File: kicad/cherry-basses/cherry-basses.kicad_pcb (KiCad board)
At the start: 2 copper layers, 175 x 53 mm, 42 parts, among them SW1.1 SPST, SW1.2 SPST, SW1.3 SPST, SW1.4 SPST, SW1.5 SPST, SW1.6 SPST, SW1.7 SPST, SW1.8 SPST, SW2.0 SPST, SW2.1 SPST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

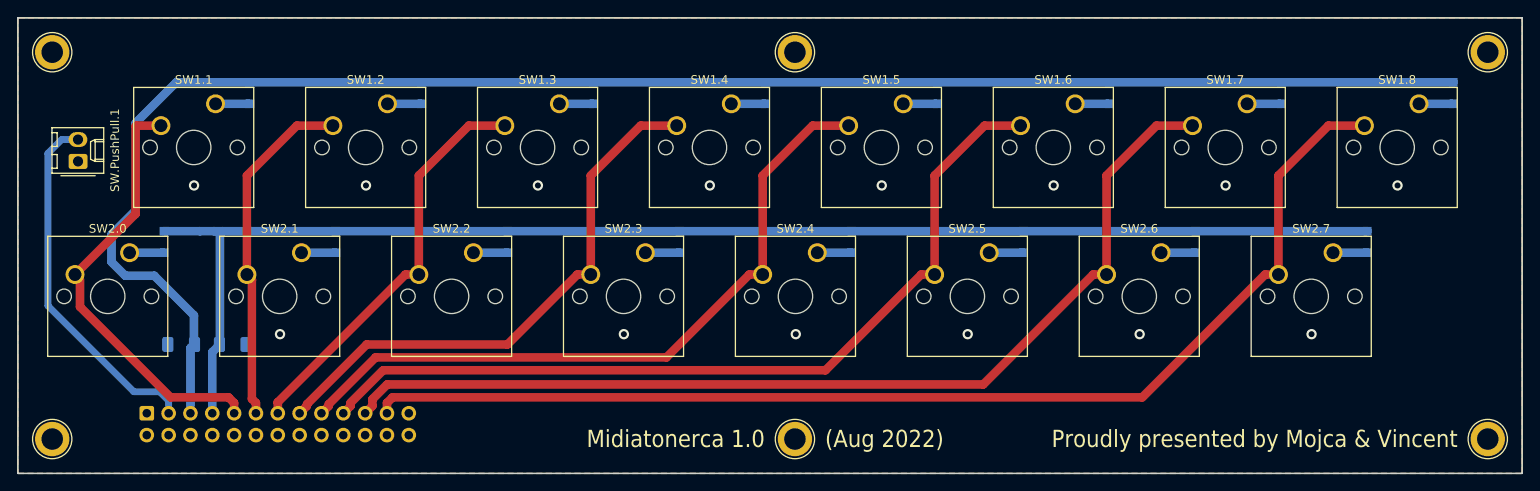
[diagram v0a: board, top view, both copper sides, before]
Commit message: cherry basses: update color, fix diode orientation, remove border from silk screen
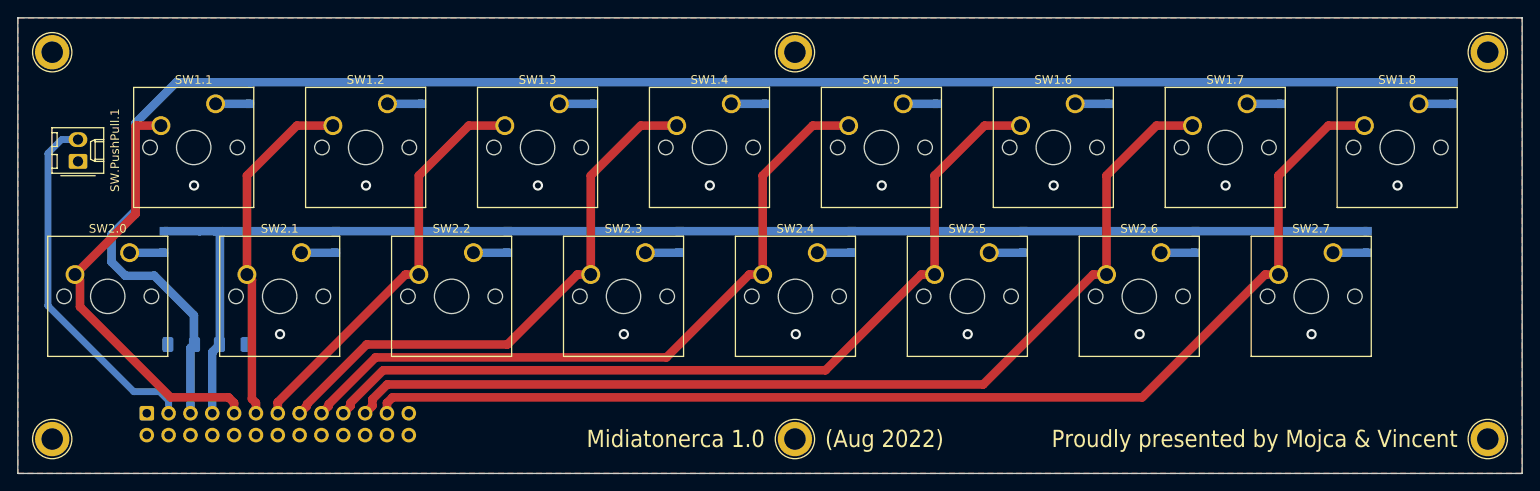
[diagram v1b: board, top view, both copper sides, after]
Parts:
- D1.1, D1.2, D1.3, D1.4, D1.5, D1.6, D1.7, D1.8, D2.0, D2.1, D2.2, D2.3, D2.4, D2.5, D2.6, D2.7: value DIODE -> 1N5819WS
- turned D1.1 to -90 degrees
- turned D1.2 to -90 degrees
- turned D1.3 to -90 degrees
- turned D1.4 to -90 degrees
- turned D1.5 to -90 degrees
- turned D1.6 to -90 degrees
- turned D1.7 to -90 degrees
- turned D1.8 to -90 degrees
- turned D2.0 to -90 degrees
- turned D2.1 to -90 degrees
- turned D2.2 to -90 degrees
- turned D2.3 to -90 degrees
- turned D2.4 to -90 degrees
- turned D2.5 to -90 degrees
- turned D2.6 to -90 degrees
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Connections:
- D1.1 pad 1: Net-(D1.1-Pad1) -> arduino_D3
- D1.1 pad 2: arduino_D3 -> Net-(D1.1-Pad2)
- D1.2 pad 1: Net-(D1.2-Pad1) -> arduino_D3
- D1.2 pad 2: arduino_D3 -> Net-(D1.2-Pad2)
- D1.3 pad 1: Net-(D1.3-Pad1) -> arduino_D3
- D1.3 pad 2: arduino_D3 -> Net-(D1.3-Pad2)
- D1.4 pad 1: Net-(D1.4-Pad1) -> arduino_D3
- D1.4 pad 2: arduino_D3 -> Net-(D1.4-Pad2)
- D1.5 pad 1: Net-(D1.5-Pad1) -> arduino_D3
- D1.5 pad 2: arduino_D3 -> Net-(D1.5-Pad2)
- D1.6 pad 1: Net-(D1.6-Pad1) -> arduino_D3
- D1.6 pad 2: arduino_D3 -> Net-(D1.6-Pad2)
- D1.7 pad 1: Net-(D1.7-Pad1) -> arduino_D3
- D1.7 pad 2: arduino_D3 -> Net-(D1.7-Pad2)
- D1.8 pad 1: Net-(D1.8-Pad1) -> arduino_D3
- D1.8 pad 2: arduino_D3 -> Net-(D1.8-Pad2)
- D2.0 pad 1: Net-(D2.0-Pad1) -> arduino_D4
- D2.0 pad 2: arduino_D4 -> Net-(D2.0-Pad2)
- D2.1 pad 1: Net-(D2.1-Pad1) -> arduino_D4
- D2.1 pad 2: arduino_D4 -> Net-(D2.1-Pad2)
- D2.2 pad 1: Net-(D2.2-Pad1) -> arduino_D4
- D2.2 pad 2: arduino_D4 -> Net-(D2.2-Pad2)
- D2.3 pad 1: Net-(D2.3-Pad1) -> arduino_D4
- D2.3 pad 2: arduino_D4 -> Net-(D2.3-Pad2)
- D2.4 pad 1: Net-(D2.4-Pad1) -> arduino_D4
- D2.4 pad 2: arduino_D4 -> Net-(D2.4-Pad2)
- D2.5 pad 1: Net-(D2.5-Pad1) -> arduino_D4
- D2.5 pad 2: arduino_D4 -> Net-(D2.5-Pad2)
- D2.6 pad 1: Net-(D2.6-Pad1) -> arduino_D4
- D2.6 pad 2: arduino_D4 -> Net-(D2.6-Pad2)
- D2.7 pad 1: Net-(D2.7-Pad1) -> arduino_D4
- D2.7 pad 2: arduino_D4 -> Net-(D2.7-Pad2)
- SW1.1 pad 1: Net-(D1.1-Pad1) -> Net-(D1.1-Pad2)
- SW1.2 pad 1: Net-(D1.2-Pad1) -> Net-(D1.2-Pad2)
- SW1.3 pad 1: Net-(D1.3-Pad1) -> Net-(D1.3-Pad2)
- SW1.4 pad 1: Net-(D1.4-Pad1) -> Net-(D1.4-Pad2)
- SW1.5 pad 1: Net-(D1.5-Pad1) -> Net-(D1.5-Pad2)
- SW1.6 pad 1: Net-(D1.6-Pad1) -> Net-(D1.6-Pad2)
- SW1.7 pad 1: Net-(D1.7-Pad1) -> Net-(D1.7-Pad2)
- SW1.8 pad 1: Net-(D1.8-Pad1) -> Net-(D1.8-Pad2)
- SW2.0 pad 1: Net-(D2.0-Pad1) -> Net-(D2.0-Pad2)
- SW2.1 pad 1: Net-(D2.1-Pad1) -> Net-(D2.1-Pad2)
- SW2.2 pad 1: Net-(D2.2-Pad1) -> Net-(D2.2-Pad2)
- SW2.3 pad 1: Net-(D2.3-Pad1) -> Net-(D2.3-Pad2)
- SW2.4 pad 1: Net-(D2.4-Pad1) -> Net-(D2.4-Pad2)
- SW2.5 pad 1: Net-(D2.5-Pad1) -> Net-(D2.5-Pad2)
- SW2.6 pad 1: Net-(D2.6-Pad1) -> Net-(D2.6-Pad2)
- SW2.7 pad 1: Net-(D2.7-Pad1) -> Net-(D2.7-Pad2)
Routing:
- net Net-(D2.2-Pad2): track 0.00 -> 8.00 mm
- net Net-(D2.2-Pad1): track 8.00 -> 0.00 mm
- net Net-(D2.7-Pad2): track 0.00 -> 4.00 mm
- net Net-(D2.7-Pad1): track 4.00 -> 0.00 mm
- net Net-(D2.6-Pad2): track 0.00 -> 4.00 mm
- net Net-(D2.6-Pad1): track 4.00 -> 0.00 mm
- net Net-(D2.5-Pad2): track 0.00 -> 4.00 mm
- net Net-(D2.5-Pad1): track 4.00 -> 0.00 mm
- net Net-(D2.4-Pad2): track 0.00 -> 4.00 mm
- net Net-(D2.4-Pad1): track 4.00 -> 0.00 mm
- net Net-(D2.3-Pad2): track 0.00 -> 4.00 mm
- net Net-(D2.3-Pad1): track 4.00 -> 0.00 mm
- net Net-(D2.1-Pad2): track 0.00 -> 4.00 mm
- net Net-(D2.1-Pad1): track 4.00 -> 0.00 mm
- net Net-(D2.0-Pad2): track 0.00 -> 4.00 mm
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
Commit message: Replace mounting holes and update components from library (cherry basses)
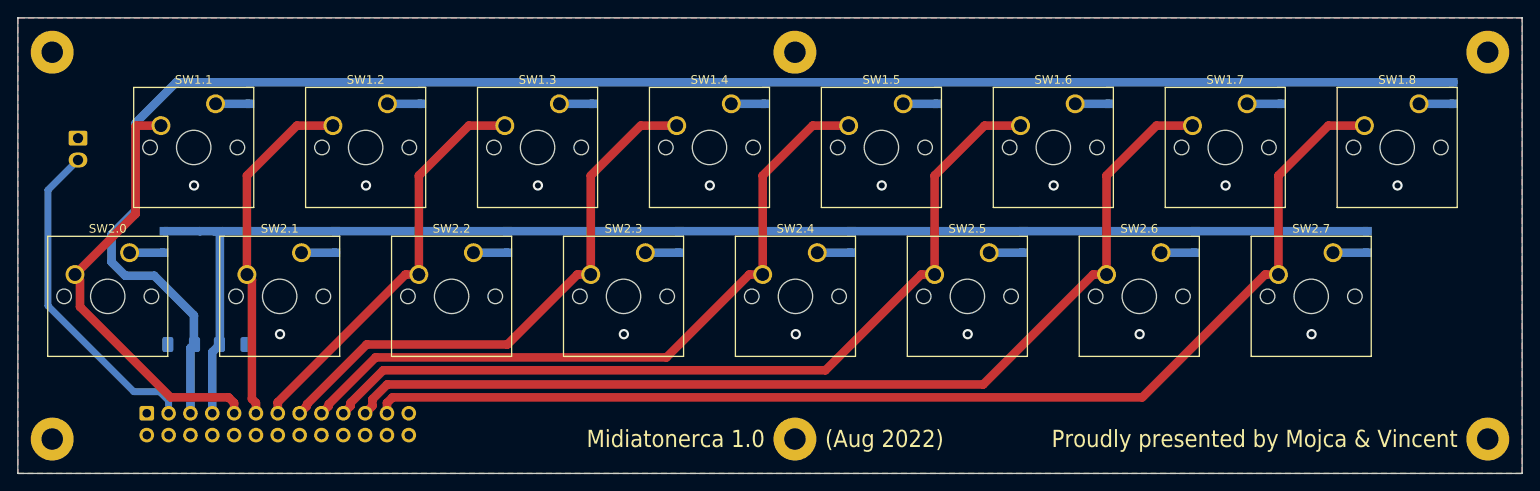
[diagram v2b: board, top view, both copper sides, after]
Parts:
- removed REF** (x6): 1pin, Connectors:1pin
- added ?: MountingHole_2.5mm_Pad, MountingHole:MountingHole_2.5mm_Pad, F.Cu at (51.0, 44.0)
- added ?: MountingHole_2.5mm_Pad, MountingHole:MountingHole_2.5mm_Pad, F.Cu at (218.0, 44.0)
- added ?: MountingHole_2.5mm_Pad, MountingHole:MountingHole_2.5mm_Pad, F.Cu at (218.0, 89.0)
- added ?: MountingHole_2.5mm_Pad, MountingHole:MountingHole_2.5mm_Pad, F.Cu at (137.4, 89.0)
- added ?: MountingHole_2.5mm_Pad, MountingHole:MountingHole_2.5mm_Pad, F.Cu at (137.4, 44.0)
- added ?: MountingHole_2.5mm_Pad, MountingHole:MountingHole_2.5mm_Pad, F.Cu at (51.0, 89.0)
- SW.PushPull.1: moved to B.Cu
- moved SW.PushPull.1 2.70 mm to (54.0, 54.0), turned to -90 degrees
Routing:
- net arduino_D2: track 42.0 -> 38.5 mm

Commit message: Add labels to the connector
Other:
- board text added: "D10"
- board text added: "D11"
- board text added: "D12"
- board text added: "D2"
- board text added: "D3"
- board text added: "D4"
- board text added: "D5"
- board text added: "D6"
- board text added: "D7"
- board text added: "D8"
- board text added: "D9"
- board text added: "GND"
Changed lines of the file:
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@@
     (property "Sheetname" "")
     (attr smd)
-    (fp_text reference "R2" (at 0 1.82 180) (layer "B.SilkS")
+    (fp_text reference "R2" (at 0 -1.82 180) (layer "B.SilkS")
       (effects (font (size 1 1) (thickness 0.15)) (justify mirror))
     )
@@
     (effects (font (size 2 1.8) (thickness 0.2)) (justify left mirror))
   )
+  (gr_text "D5" (at 72.18 82.5 270) (layer "B.SilkS")
+    (effects (font (size 1 1) (thickness 0.15)) (justify left mirror))
+  )
   (gr_text "(Aug 2022)" (at 140.9 89) (layer "B.SilkS")
     (effects (font (size 2 1.8) (thickness 0.2)) (justify right mirror))
+  )
+  (gr_text "D9" (at 82.34 82.5 270) (layer "B.SilkS")
+    (effects (font (size 1 1) (thickness 0.15)) (justify left mirror))
+  )
+  (gr_text "D7" (at 77.26 82.5 270) (layer "B.SilkS")
+    (effects (font (size 1 1) (thickness 0.15)) (justify left mirror))
+  )
+  (gr_text "GND" (at 92.5 82.5 270) (layer "B.SilkS")
+    (effects (font (size 1 1) (thickness 0.15)) (justify left mirror))
+  )
+  (gr_text "D4" (at 69.64 82.5 270) (layer "B.SilkS")
+    (effects (font (size 1 1) (thickness 0.15)) (justify left mirror))
+  )
+  (gr_text "D8" (at 79.8 82.5 270) (layer "B.SilkS")
+    (effects (font (size 1 1) (thickness 0.15)) (justify left mirror))
+  )
+  (gr_text "D12" (at 89.96 82.5 270) (layer "B.SilkS")
+    (effects (font (size 1 1) (thickness 0.15)) (justify left mirror))
+  )
+  (gr_text "D6" (at 74.72 82.5 270) (layer "B.SilkS")
+    (effects (font (size 1 1) (thickness 0.15)) (justify left mirror))
+  )
+  (gr_text "D3" (at 67.1 82.5 270) (layer "B.SilkS")
+    (effects (font (size 1 1) (thickness 0.15)) (justify left mirror))
   )
   (gr_text "Proudly presented by Mojca & Vincent" (at 214.5 89) (layer "B.SilkS")
     (effects (font (size 2 1.8) (thickness 0.2)) (justify left mirror))
   )
+  (gr_text "D11" (at 87.42 82.5 270) (layer "B.SilkS")
+    (effects (font (size 1 1) (thickness 0.15)) (justify left mirror))
+  )
+  (gr_text "D10" (at 84.88 82.5 270) (layer "B.SilkS")
+    (effects (font (size 1 1) (thickness 0.15)) (justify left mirror))
+  )
+  (gr_text "D2" (at 64.56 82.5 270) (layer "B.SilkS")
+    (effects (font (size 1 1) (thickness 0.15)) (justify left mirror))
+  )
   (gr_text "Proudly presented by Mojca & Vincent" (at 214.5 89) (layer "F.SilkS")

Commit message: Add osh logo
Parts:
- added REF**: OSHW-Logo2_14.6x12mm_SilkScreen, Symbol:OSHW-Logo2_14.6x12mm_SilkScreen, F.Cu at (213.0, 72.5)
- added REF**: OSHW-Logo2_14.6x12mm_SilkScreen, Symbol:OSHW-Logo2_14.6x12mm_SilkScreen, B.Cu at (213.0, 72.5)
